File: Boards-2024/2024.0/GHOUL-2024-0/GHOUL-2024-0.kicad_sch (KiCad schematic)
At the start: 82 parts, among them J1 USB_C_Receptacle_USB2.0, J2 U.FL, J3 SOICbite, J4 Conn_01x03_Pin, Q1 Q_NMOS_GSD, SW2 SLIDE, U1 MCU_RaspberryPi_RP2040_RP2040, U11 MAX-M10S, U2 TVS1800DRVR, U3 USBLC6-2SC6, U4 TPS2121RUXR, U5 W25Q128JVS, U6 LT6703CDC-3, U7 DRF1262TL, U8 MB85RS1MT, U9 MS5607-02BA, Y1 12MHz

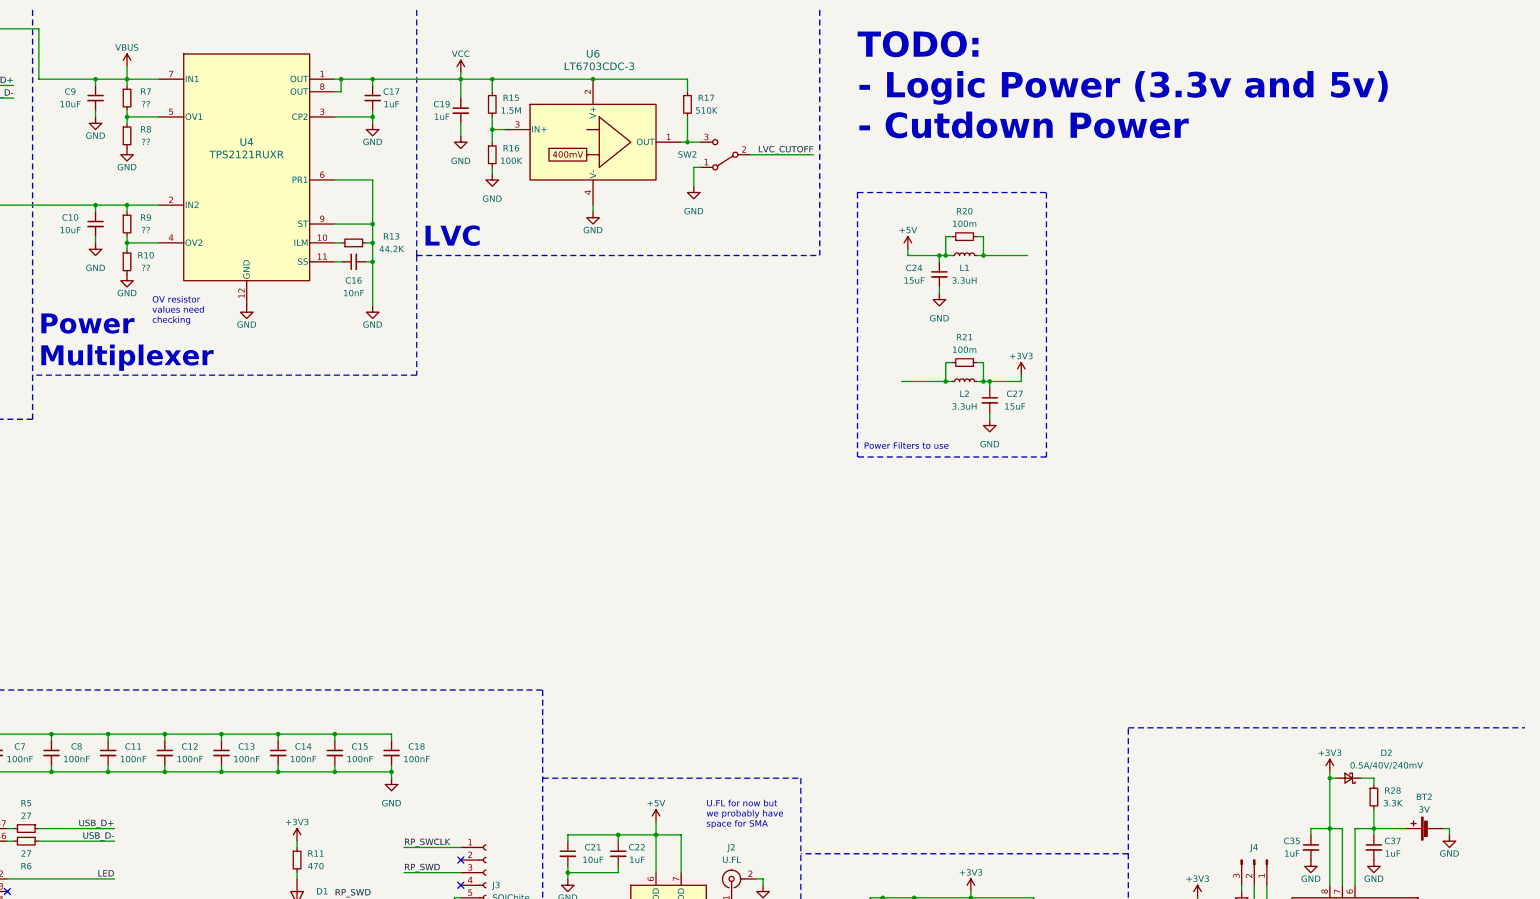
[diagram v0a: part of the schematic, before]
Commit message: added buck converter to logic board
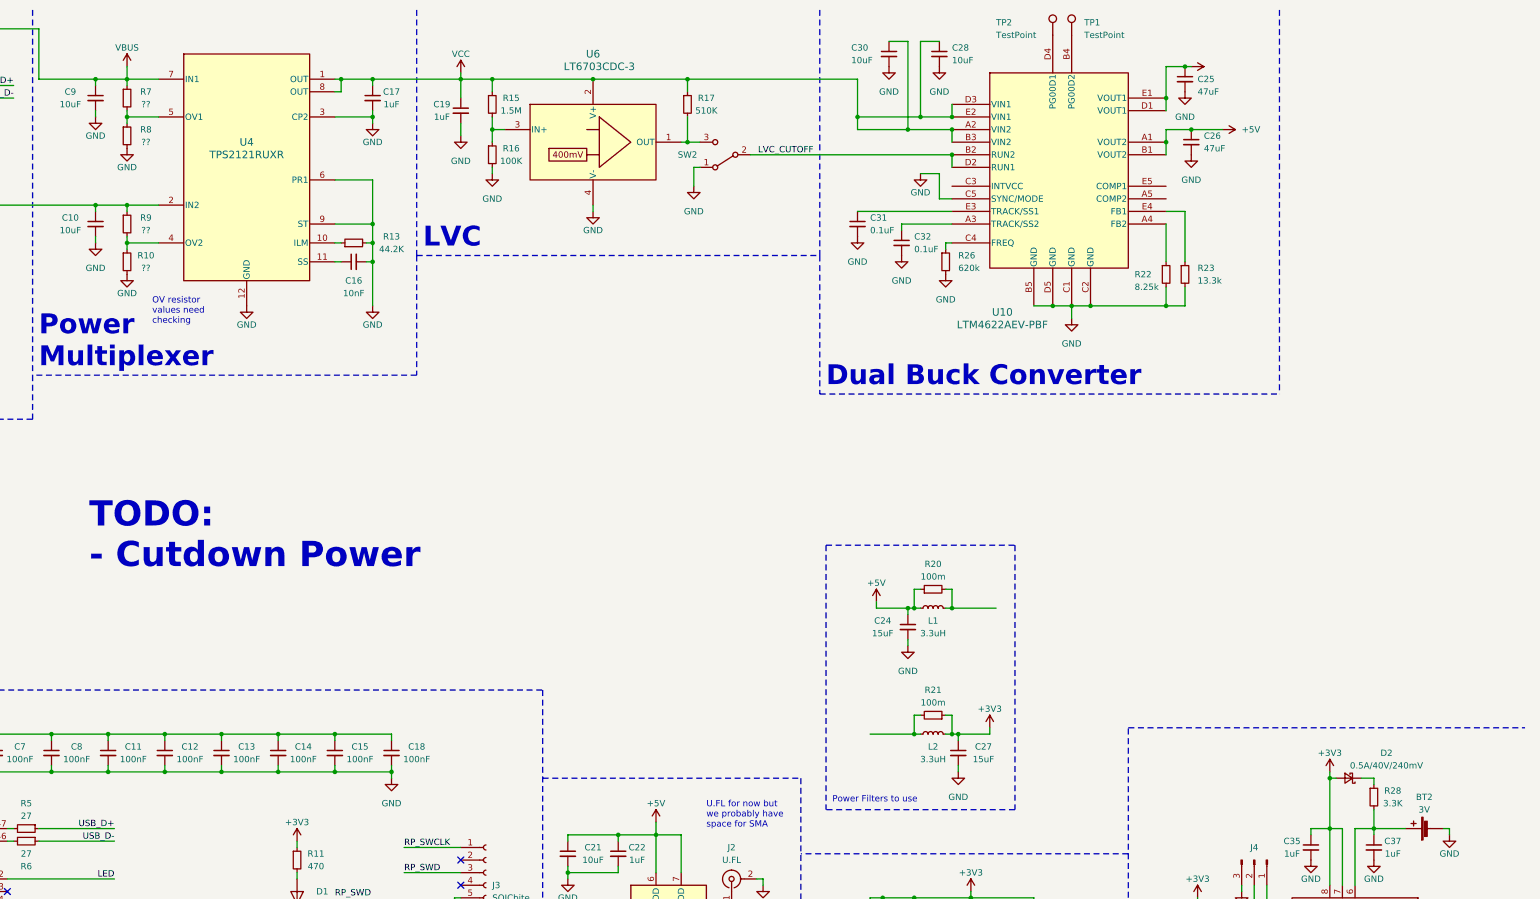
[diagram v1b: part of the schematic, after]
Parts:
- added C25, C26: 47uF, symbol Device:C_Small
- added C28, C30: 10uF, symbol Device:C_Small
- added C31, C32: 0.1uF, symbol Device:C_Small
- added R22: 8.25k, symbol Device:R_Small
- added R23: 13.3k, symbol Device:R_Small
- added R26: 620k, symbol Device:R_Small
- added TP1, TP2: TestPoint, symbol Connector:TestPoint
- added U10: LTM4622AEV-PBF, LGA25_6P25X6P25_ADI, symbol 2024-02-03_22-46-21:LTM4622AEV-PBF
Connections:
- net +5V: now also C26.1, U10.A1 (VOUT2), U10.B1 (VOUT2)
- net GND: now also C25.2, C26.2, C28.2, C30.2, C31.2, C32.2, R22.2, R23.2, R26.2, U10.B5 (GND), U10.C1 (GND), U10.C2 (GND), U10.C5 (SYNC/MODE), U10.D5 (GND)
- net LVC_CUTOFF: now also U10.B2 (RUN2), U10.D2 (RUN1)
- net VCC: now also C28.1, C30.1, U10.A2 (VIN2), U10.B3 (VIN2), U10.D3 (VIN1), U10.E2 (VIN1)
- new net: TP2.1, U10.D4 (PG00D1)
- new net: TP1.1, U10.B4 (PG00D2)
- new net: C32.1, U10.A3 (TRACK/SS2)
- new net: R23.1, U10.E4 (FB1)
- new net: R26.1, U10.C4 (FREQ)
- new net: C31.1, U10.E3 (TRACK/SS1)
- new net: R22.1, U10.A4 (FB2)
- new net: U11.10 (GND), U11.12 (GND)
- new net +3.3V: C25.1, U10.D1 (VOUT1), U10.E1 (VOUT1)
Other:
- note added: "Dual Buck Converter"
- note added: "TODO: - Cutdown Power"
- note removed: "TODO: - Logic Power (3.3v and 5v) - Cutdown Power"
- moved on the sheet: C24, C27, L1, L2, R20, R21

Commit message: started layout
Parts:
- C25, C26, C28, C30, C31, C32: footprint (none) -> Capacitor_SMD:C_0603_1608Metric
- R22, R23, R26: footprint (none) -> Resistor_SMD:R_0603_1608Metric
- TP1, TP2: footprint (none) -> TestPoint:TestPoint_Keystone_5000-5004_Miniature
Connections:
- new net: U11.10 (GND), U11.12 (GND)
- no-connect marks 28 -> 31
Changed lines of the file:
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@@
   (no_connect (at 358.14 217.17))
   (no_connect (at 41.91 53.34))
+  (no_connect (at 335.28 50.8))
   (no_connect (at 285.75 204.47))
   (no_connect (at 152.4 231.14))
@@
   (no_connect (at 226.06 257.81))
   (no_connect (at 101.6 200.66))
+  (no_connect (at 335.28 48.26))
+  (no_connect (at 292.1 48.26))
   (no_connect (at 101.6 190.5))
   (no_connect (at 226.06 260.35))
@@
       (effects (font (size 1.27 1.27)) (justify left))
     )
-    (property "Footprint" "" (at 279.4 21.59 0)
+    (property "Footprint" "Capacitor_SMD:C_0603_1608Metric" (at 279.4 21.59 0)
       (effects (font (size 1.27 1.27)) hide)
     )
@@
       (effects (font (size 1.27 1.27)) (justify left))
     )
-    (property "Footprint" "" (at 317.5 17.78 0)
+    (property "Footprint" "TestPoint:TestPoint_Keystone_5000-5004_Miniature" (at 317.5 17.78 0)
       (effects (font (size 1.27 1.27)) hide)
     )
@@
       (effects (font (size 1.27 1.27)) (justify left))
     )
-    (property "Footprint" "" (at 340.36 39.37 0)
+    (property "Footprint" "Capacitor_SMD:C_0603_1608Metric" (at 340.36 39.37 0)
       (effects (font (size 1.27 1.27)) hide)
     )
@@
       (effects (font (size 1.27 1.27)) (justify left))
     )
-    (property "Footprint" "" (at 321.31 17.78 0)
+    (property "Footprint" "TestPoint:TestPoint_Keystone_5000-5004_Miniature" (at 321.31 17.78 0)
       (effects (font (size 1.27 1.27)) hide)
     )
@@
       (effects (font (size 1.27 1.27)) (justify left))
     )
-    (property "Footprint" "" (at 339.09 26.67 0)
+    (property "Footprint" "Capacitor_SMD:C_0603_1608Metric" (at 339.09 26.67 0)
       (effects (font (size 1.27 1.27)) hide)
     )
@@
       (effects (font (size 1.27 1.27)) (justify left))
     )
-    (property "Footprint" "" (at 281.94 59.69 0)
+    (property "Footprint" "Capacitor_SMD:C_0603_1608Metric" (at 281.94 59.69 0)
       (effects (font (size 1.27 1.27)) hide)
     )
@@
       (effects (font (size 1.27 1.27)) (justify left))
     )
-    (property "Footprint" "" (at 289.56 21.59 0)
+    (property "Footprint" "Capacitor_SMD:C_0603_1608Metric" (at 289.56 21.59 0)
       (effects (font (size 1.27 1.27)) hide)
     )
@@
       (effects (font (size 1.27 1.27)) (justify left))
     )
-    (property "Footprint" "" (at 339.09 66.04 0)
+    (property "Footprint" "Resistor_SMD:R_0603_1608Metric" (at 339.09 66.04 0)
       (effects (font (size 1.27 1.27)) hide)
     )
@@
       (effects (font (size 1.27 1.27)) (justify left))
     )
-    (property "Footprint" "" (at 290.83 63.5 0)
+    (property "Footprint" "Resistor_SMD:R_0603_1608Metric" (at 290.83 63.5 0)
       (effects (font (size 1.27 1.27)) hide)
     )
@@
       (effects (font (size 1.27 1.27)) (justify left))
     )
-    (property "Footprint" "" (at 273.05 55.88 0)
+    (property "Footprint" "Capacitor_SMD:C_0603_1608Metric" (at 273.05 55.88 0)
       (effects (font (size 1.27 1.27)) hide)
     )
@@
       (effects (font (size 1.27 1.27)) (justify left))
     )
-    (property "Footprint" "" (at 335.28 66.04 0)
+    (property "Footprint" "Resistor_SMD:R_0603_1608Metric" (at 335.28 66.04 0)
       (effects (font (size 1.27 1.27)) hide)
     )

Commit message: starting board layout
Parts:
- U10: footprint LGA25_6P25X6P25_ADI -> GHOUL2024:LGA25_6P25X6P25_ADI
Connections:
- new net: U11.10 (GND), U11.12 (GND)
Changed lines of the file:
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@@
       (effects (font (size 1.524 1.524)))
     )
-    (property "Footprint" "LGA25_6P25X6P25_ADI" (at 313.69 45.72 0)
+    (property "Footprint" "GHOUL2024:LGA25_6P25X6P25_ADI" (at 313.69 45.72 0)
       (effects (font (size 1.27 1.27) italic) hide)
     )

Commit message: finished connecting everything
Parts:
- added D3, D4, D5, D6: LED, LED_SMD:LED_0603_1608Metric, symbol Device:LED
- added Q2, Q3, Q4, Q5: Q_NMOS_GSD, Package_TO_SOT_SMD:SOT-23-3, symbol Device:Q_NMOS_GSD
- added R27, R29, R30, R31: 470, Resistor_SMD:R_0603_1608Metric, symbol Device:R_Small
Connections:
- net +3.3V is gone; now on an unnamed net: C25.1, U10.D1 (VOUT1), U10.E1 (VOUT1)
- net +3V3: now also R27.1, R29.1, R30.1, R31.1
- net +5V: no longer C26.1, U10.A1 (VOUT2), U10.B1 (VOUT2)
- net GND: now also Q2.2 (S), Q3.2 (S), Q4.2 (S), Q5.2 (S)
- net at L1.2, R20.2: now also C26.1, U10.A1 (VOUT2), U10.B1 (VOUT2)
- net LED2: now reaches U1.3 (GPIO1)
- net LED2: now also Q4.1 (G)
- net LED3: now reaches U1.4 (GPIO2)
- net LED3: now also Q2.1 (G)
- net LED4: now reaches U1.5 (GPIO3)
- net LED4: now also Q5.1 (G)
- net LED5: now reaches U1.6 (GPIO4)
- net LED5: now also Q1.1 (G)
- net LED renamed LED1
- net LED1: now also Q3.1 (G); no longer Q1.1 (G)
- new net: D5.2 (A), R30.2
- new net: D3.2 (A), R27.2
- new net: D4.1 (K), Q3.3 (D)
- new net: D4.2 (A), R29.2
- new net: D3.1 (K), Q2.3 (D)
- new net: D6.1 (K), Q5.3 (D)
- new net: D6.2 (A), R31.2
- new net: D5.1 (K), Q4.3 (D)
- new net: U11.10 (GND), U11.12 (GND)
- no-connect marks 31 -> 27
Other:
- note added: "LEDs"
- note removed: "LED"
- moved on the sheet: C24, C26, C27, D1, L1, L2, Q1, R11, R20, R21

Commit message: finished board
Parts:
- added J10: Conn_01x04, Connector_PinHeader_2.54mm:PinHeader_1x04_P2.54mm_Vertical, symbol Connector_Generic:Conn_01x04
- added J5, J9: Conn_01x04, Connector_Molex:Molex_SL_171971-0004_1x04_P2.54mm_Vertical, symbol Connector_Generic:Conn_01x04
- added J6: Conn_01x03, Connector_Molex:Molex_SL_171971-0003_1x03_P2.54mm_Vertical, symbol Connector_Generic:Conn_01x03
- added J7, J8: Conn_01x02, Connector_Molex:Molex_SL_171971-0002_1x02_P2.54mm_Vertical, symbol Connector_Generic:Conn_01x02
- added Q6, Q7: Q_NMOS_GSD, Package_TO_SOT_SMD:SC-59, symbol Device:Q_NMOS_GSD
- added R32: 4.7k, Resistor_SMD:R_0603_1608Metric, symbol Device:R_Small
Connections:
- net +3V3: now also J6.2 (Pin_2), R32.1
- net +5V: now also J5.3 (Pin_3), J7.1 (Pin_1), J8.1 (Pin_1)
- net GND: now also J5.4 (Pin_4), J6.3 (Pin_3), J9.1 (Pin_1), Q6.2 (S), Q7.2 (S)
- net LED3: now also U1.9 (GPIO7); no longer U1.4 (GPIO2)
- net LED4: now also U1.15 (GPIO12); no longer U1.5 (GPIO3)
- net HEATER1: now reaches U1.17 (GPIO14)
- net HEATER1: now also Q6.1 (G)
- net HEATER2: now reaches U1.18 (GPIO15)
- net HEATER2: now also Q7.1 (G)
- net GPIO16: now reaches U1.27 (GPIO16)
- net GPIO16: now also J10.3 (Pin_3)
- net GPIO19: now reaches U1.30 (GPIO19)
- net GPIO19: now also J10.4 (Pin_4)
- net PGOOD_CUT: now reaches U1.34 (GPIO22)
- net PGOOD_CUT: now also J9.4 (Pin_4)
- net DATA_CUT: now reaches U1.35 (GPIO23)
- net DATA_CUT: now also J9.3 (Pin_3)
- net CUT_CURR: now reaches U1.40 (GPIO28_ADC2)
- net CUT_CURR: now also J9.2 (Pin_2)
- net SERVO_PWM: now reaches U1.7 (GPIO5)
- net SERVO_PWM: now also J5.2 (Pin_2)
- net TEMP: now reaches U1.8 (GPIO6)
- net TEMP: now also J6.1 (Pin_1), R32.2
- new net: J8.2 (Pin_2), Q7.3 (D)
- new net: J7.2 (Pin_2), Q6.3 (D)
- new net: U11.10 (GND), U11.12 (GND)
- new net GPIO2: J10.1 (Pin_1), U1.4 (GPIO2)
- new net GPIO3: J10.2 (Pin_2), U1.5 (GPIO3)
- no-connect marks 27 -> 18
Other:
- note added: "Cut Connector"
- note added: "Heaters"
- note added: "Power filters"
- note added: "Servo"
- note added: "Temp Probe"
- note removed: "Power Filters to use"
- moved on the sheet: D1, D6, Q1, Q5, R11, R31

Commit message: ready for shipman review
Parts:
- C25, C26: footprint Capacitor_SMD:C_0603_1608Metric -> Capacitor_SMD:C_0805_2012Metric
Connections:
- new net: U11.10 (GND), U11.12 (GND)
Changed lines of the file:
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@@
       (effects (font (size 1.27 1.27)) (justify left))
     )
-    (property "Footprint" "Capacitor_SMD:C_0603_1608Metric" (at 344.17 46.99 0)
+    (property "Footprint" "Capacitor_SMD:C_0805_2012Metric" (at 344.17 46.99 0)
       (effects (font (size 1.27 1.27)) hide)
     )
@@
       (effects (font (size 1.27 1.27)) (justify left))
     )
-    (property "Footprint" "Capacitor_SMD:C_0603_1608Metric" (at 339.09 26.67 0)
-      (effects (font (size 1.27 1.27)) hide)
-    )
+    (property "Footprint" "Capacitor_SMD:C_0805_2012Metric" (at 339.09 26.67 0)
+      (effects (font (size 1.27 1.27)) hide)
+    )

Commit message: ordered GHOUL 2024.0
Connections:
- new net: U11.10 (GND), U11.12 (GND)
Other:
- note removed: "TODO: - Cutdown Power"
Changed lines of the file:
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@@
     (effects (font (size 3 3) (thickness 0.8) bold) (justify left bottom))
-  )
-  (text "TODO:\n- Cutdown Power" (at 511.81 77.47 0)
-    (effects (font (size 5.08 5.08) (thickness 1.016) bold (color 255 0 0 1)) (justify left bottom))
   )
   (text "LEDs" (at 24.13 92.71 0)
